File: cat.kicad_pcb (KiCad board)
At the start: 2 copper layers, 74.5 x 94 mm, 14 parts, among them Q1 NPN, SW1 SW_Push, SW2 SW_Push

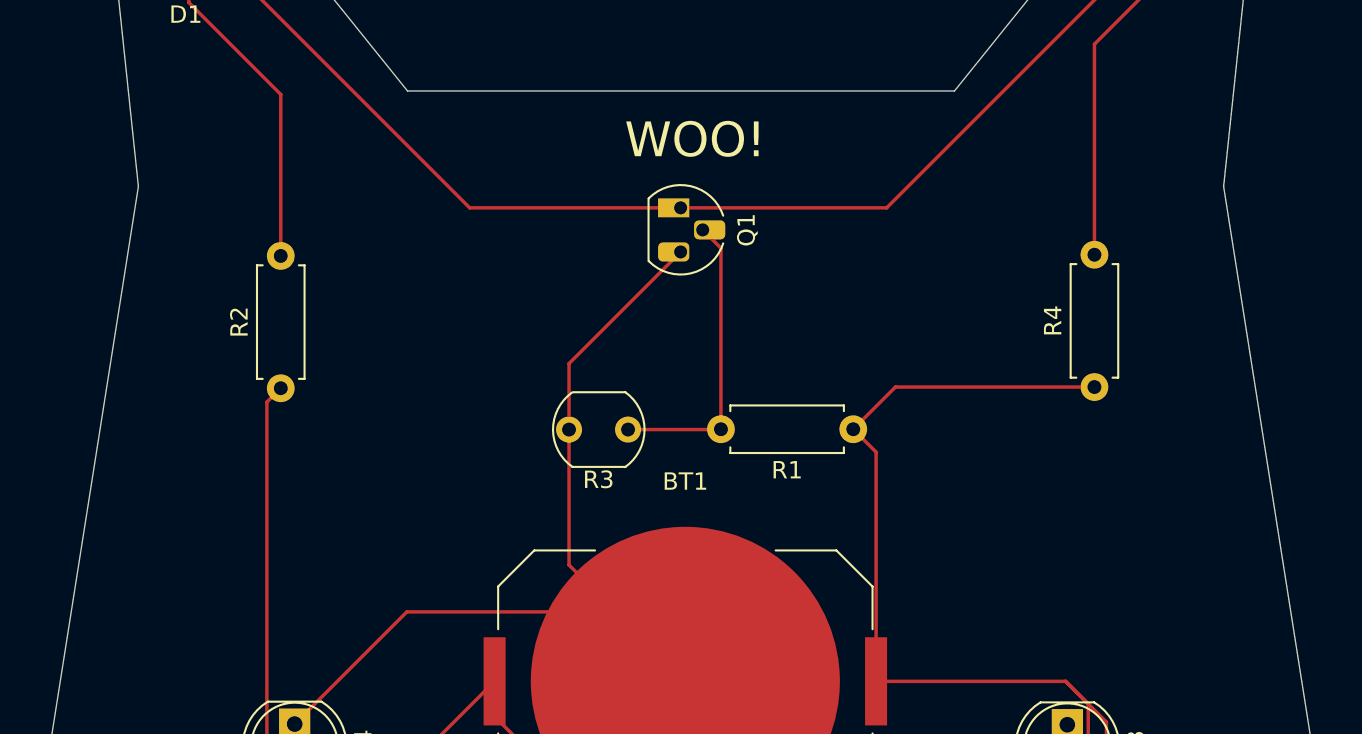
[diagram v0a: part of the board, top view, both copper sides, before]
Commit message: add more silkscreen
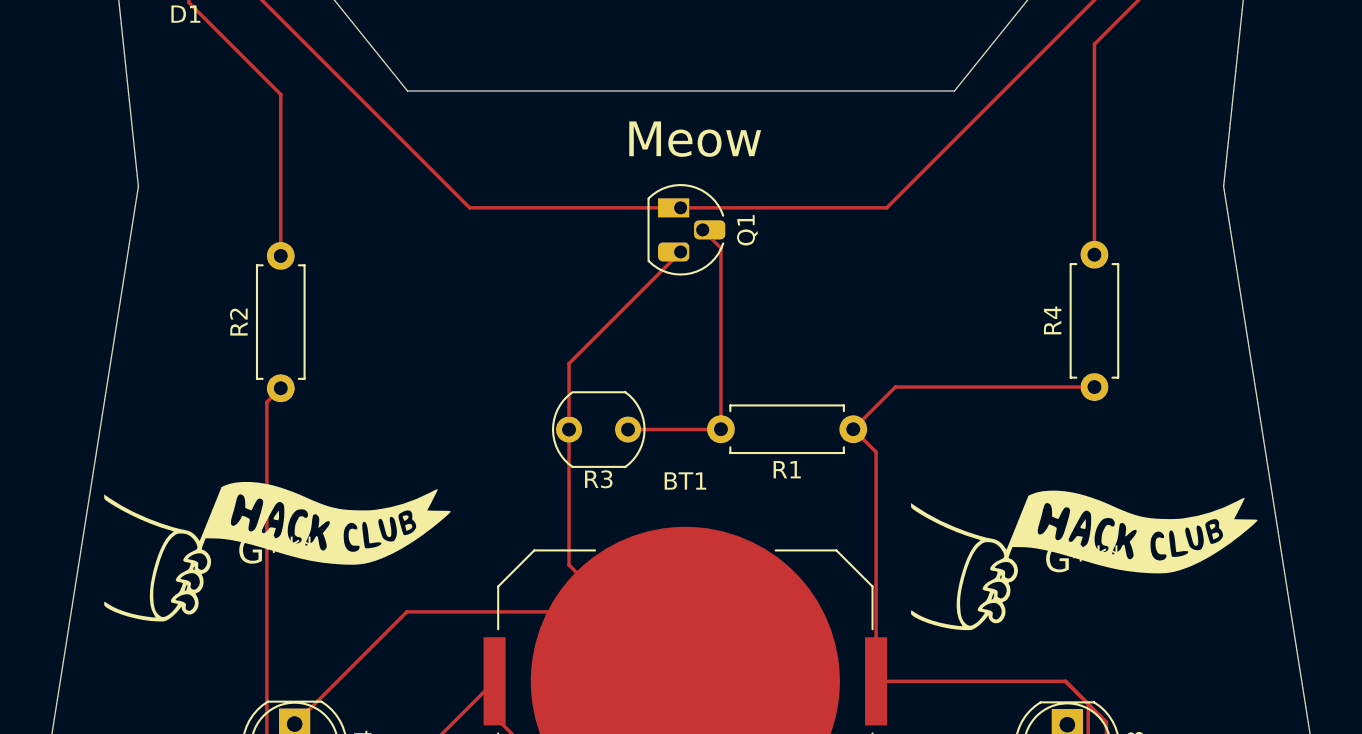
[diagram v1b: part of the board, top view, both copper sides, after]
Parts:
- added G***: LOGO, LOGO, F.Cu at (115.5, 92.0)
- added G***: LOGO, LOGO, F.Cu at (162.0, 92.5)
- added G***: LOGO, LOGO, B.Cu at (157.5, 74.0)
- added G***: LOGO, LOGO, B.Cu at (118.0, 74.5)
- added G***: LOGO, LOGO, B.Cu at (139.5, 103.0)
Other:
- board text added: "Meow"
- board text added: "Meow Made for Solder by"
- board text removed: "WOO!"
